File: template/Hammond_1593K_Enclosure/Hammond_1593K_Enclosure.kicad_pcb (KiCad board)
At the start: 2 copper layers, 56.6 x 57.7 mm, 4 parts

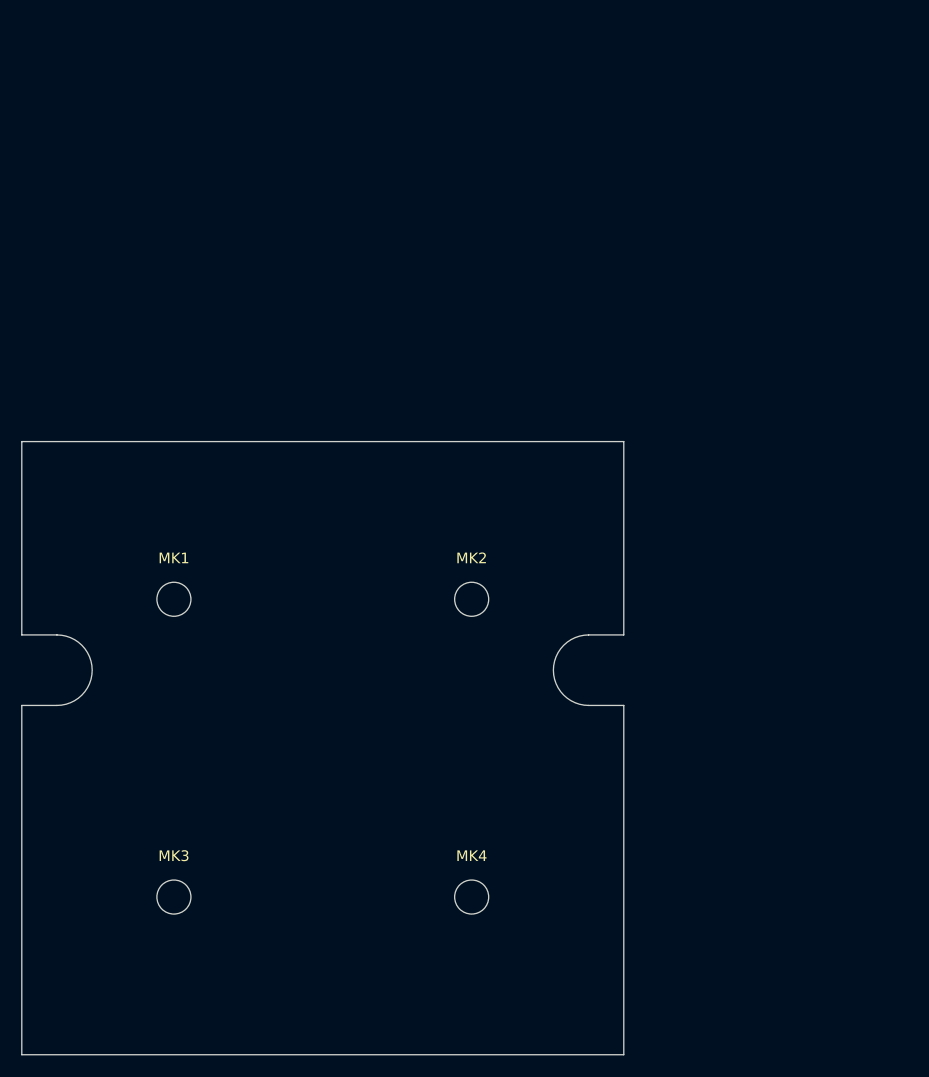
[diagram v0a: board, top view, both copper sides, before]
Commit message: fix: change original libs; add: new components
- Fix LIS3DH pins positions;
- Add ATmega164P symbol;
- Add 3D model to the L_Wuerth_HCM-7050;
- Add parameters for R_RES (Assembly...).
- Add parameters for R_RES and C_CAP;
- Fix SOIC-8 package 3D model;
- Add new parameters for many symbols;
- Change text height from 70 mil to 50 mil;
- Add solder mask expansion for 2-contact jumpers;
- Change thermopad vias of QFN-20-1EP_3x3mm_P0.45mm_EP1.6x1.6mm_ThermalVias;
- Add D_SMAF footprint;
- Fillet silk for C_1206;
-Rectangle silk for R_1206;
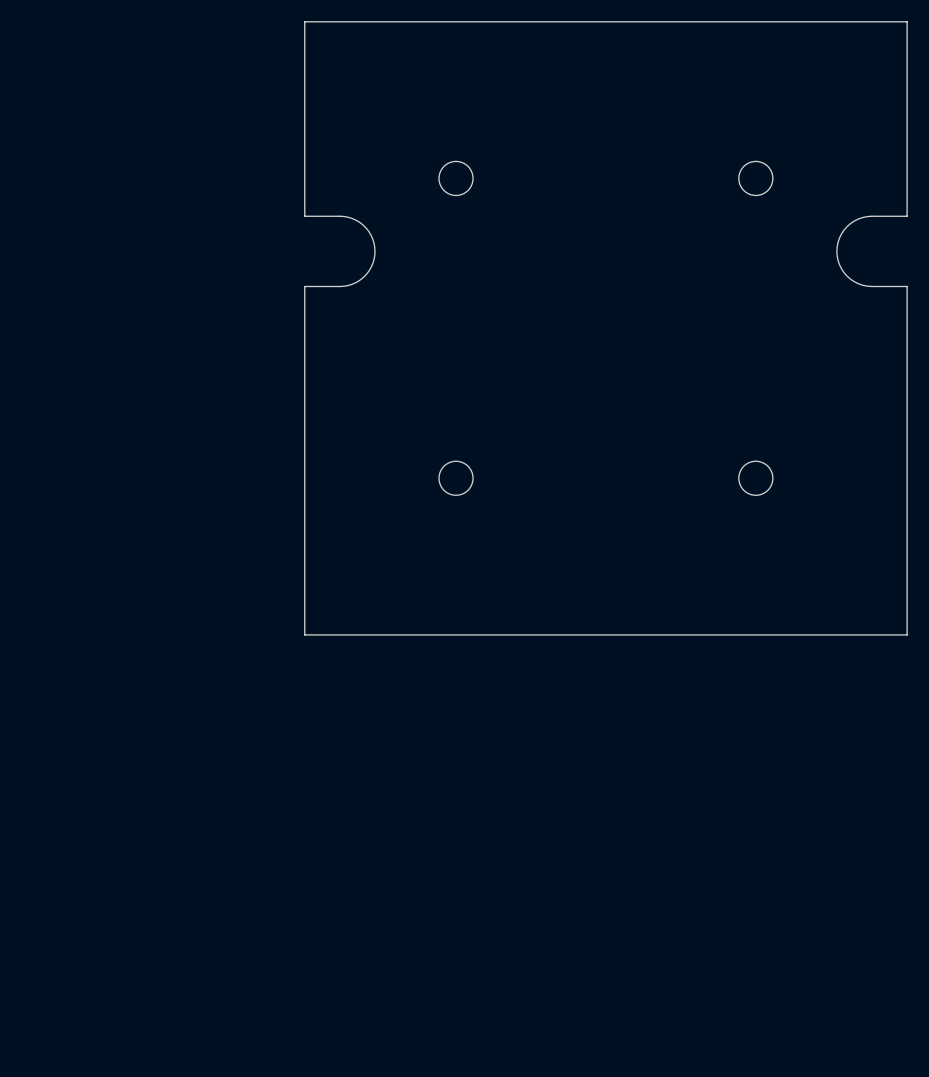
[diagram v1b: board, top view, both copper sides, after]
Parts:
- removed MK1, MK2, MK3, MK4: Mounting_Hole, Mounting_Holes:MountingHole_3.2mm_M3_ISO7380
- added MH1: MountingHole_3.2mm_M3_ISO7380, MountingHole:MountingHole_3.2mm_M3_ISO7380, F.Cu at (114.2, 57.1)
- added MH2: MountingHole_3.2mm_M3_ISO7380, MountingHole:MountingHole_3.2mm_M3_ISO7380, F.Cu at (114.2, 85.3)
- added MH3: MountingHole_3.2mm_M3_ISO7380, MountingHole:MountingHole_3.2mm_M3_ISO7380, F.Cu at (142.4, 57.1)
- added MH4: MountingHole_3.2mm_M3_ISO7380, MountingHole:MountingHole_3.2mm_M3_ISO7380, F.Cu at (142.4, 85.3)
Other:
- outline, holes or cut-outs redrawn
- board text removed: "NO CONNECTORS"
- board text removed: "RIGHT ANGLE CONNECTORS ON FRONT AND BACK ONLY"
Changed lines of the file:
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@@
-(kicad_pcb (version 20210126) (generator pcbnew)
+(kicad_pcb (version 20211014) (generator pcbnew)
   (general
     (thickness 1.6)
@@
     (33 "F.Adhes" user "F.Adhesive")
     (35 "F.Paste" user)
+    (36 "B.SilkS" user "B.Silkscreen")
     (37 "F.SilkS" user "F.Silkscreen")
+    (38 "B.Mask" user)
     (39 "F.Mask" user)
     (40 "Dwgs.User" user "User.Drawings")
@@
     (44 "Edge.Cuts" user)
     (45 "Margin" user)
+    (46 "B.CrtYd" user "B.Courtyard")
     (47 "F.CrtYd" user "F.Courtyard")
+    (48 "B.Fab" user)
     (49 "F.Fab" user)
   )
   (setup
-    (aux_axis_origin 130 100)
-    (grid_origin 130 100)
+    (stackup
+      (layer "F.SilkS" (type "Top Silk Screen"))
+      (layer "F.Paste" (type "Top Solder Paste"))
+      (layer "F.Mask" (type "Top Solder Mask") (color "Green") (thickness 0.01))
+      (layer "F.Cu" (type "copper") (thickness 0.035))
+      (layer "dielectric 1" (type "core") (thickness 1.51) (material "FR4") (epsilon_r 4.5) (loss_tangent 0.02))
+      (layer "B.Cu" (type "copper") (thickness 0.035))
+      (layer "B.Mask" (type "Bottom Solder Mask") (color "Green") (thickness 0.01))
+      (layer "B.SilkS" (type "Bottom Silk Screen"))
+      (copper_finish "None")
+      (dielectric_constraints no)
+    )
+    (pad_to_mask_clearance 0)
+    (aux_axis_origin 100 100)
+    (grid_origin 100 100)
     (pcbplotparams
       (layerselection 0x00010a8_80000001)
@@
   )
   (net 0 "")
-  (net 1 "Net-(MK1-Pad1)")
-  (net 2 "Net-(MK2-Pad1)")
-  (net 3 "Net-(MK3-Pad1)")
-  (net 4 "Net-(MK4-Pad1)")
-  (footprint "Mounting_Holes:MountingHole_3.2mm_M3_ISO7380" locked (layer "F.Cu")
-    (at 87.695 96.647)
+  (footprint "MountingHole:MountingHole_3.2mm_M3_ISO7380" locked (layer "F.Cu")
+    (at 142.418 85.268)
     (descr "Mounting Hole 3.2mm, no annular, M3, ISO7380")
     (tags "mounting hole 3.2mm no annular m3 iso7380")
-    (attr exclude_from_pos_files exclude_from_bom)
-    (fp_text reference "MK1" (at 0 -3.85) (layer "F.SilkS")
+    (attr board_only exclude_from_pos_files exclude_from_bom)
+    (fp_text reference "MH4" (at 0 -3.85) (layer "F.Fab") hide
       (effects (font (size 1 1) (thickness 0.15)))
     )
-    (fp_text value "Mounting_Hole" (at 0 3.85) (layer "F.Fab")
+    (fp_text value "MountingHole_3.2mm_M3_ISO7380" (at 0 3.85) (layer "F.Fab") hide
       (effects (font (size 1 1) (thickness 0.15)))
     )
-    (fp_text user "${REFERENCE}" (at 0.3 0) (layer "F.Fab")
+    (fp_text user "${REFERENCE}" (at 0.3 0) (layer "F.Fab") hide
       (effects (font (size 1 1) (thickness 0.15)))
     )
     (fp_circle (center 0 0) (end 2.85 0) (layer "Cmts.User") (width 0.15) (fill none))
     (fp_circle (center 0 0) (end 3.1 0) (layer "F.CrtYd") (width 0.05) (fill none))
-    (pad "1" np_thru_hole circle (at 0 0) (locked) (size 3.2 3.2) (drill 3.2) (layers *.Cu *.Mask)
-      (net 1 "Net-(MK1-Pad1)"))
+    (pad "" np_thru_hole circle locked (at 0 0) (size 3.2 3.2) (drill 3.2) (layers *.Cu *.Mask))
   )
-  (footprint "Mounting_Holes:MountingHole_3.2mm_M3_ISO7380" locked (layer "F.Cu")
-    (at 115.695 96.647)
+  (footprint "MountingHole:MountingHole_3.2mm_M3_ISO7380" locked (layer "F.Cu")
+    (at 114.224 85.268)
     (descr "Mounting Hole 3.2mm, no annular, M3, ISO7380")
     (tags "mounting hole 3.2mm no annular m3 iso7380")
-    (attr exclude_from_pos_files exclude_from_bom)
-    (fp_text reference "MK2" (at 0 -3.85) (layer "F.SilkS")
+    (attr board_only exclude_from_pos_files exclude_from_bom)
+    (fp_text reference "MH2" (at 0 -3.85) (layer "F.Fab") hide
       (effects (font (size 1 1) (thickness 0.15)))
     )
-    (fp_text value "Mounting_Hole" (at 0 3.85) (layer "F.Fab")
+    (fp_text value "MountingHole_3.2mm_M3_ISO7380" (at 0 3.85) (layer "F.Fab") hide
       (effects (font (size 1 1) (thickness 0.15)))
     )
-    (fp_text user "${REFERENCE}" (at 0.3 0) (layer "F.Fab")
+    (fp_text user "${REFERENCE}" (at 0.3 0) (layer "F.Fab") hide
       (effects (font (size 1 1) (thickness 0.15)))
     )
     (fp_circle (center 0 0) (end 2.85 0) (layer "Cmts.User") (width 0.15) (fill none))
     (fp_circle (center 0 0) (end 3.1 0) (layer "F.CrtYd") (width 0.05) (fill none))
-    (pad "1" np_thru_hole circle (at 0 0) (locked) (size 3.2 3.2) (drill 3.2) (layers *.Cu *.Mask)
-      (net 2 "Net-(MK2-Pad1)"))
+    (pad "" np_thru_hole circle locked (at 0 0) (size 3.2 3.2) (drill 3.2) (layers *.Cu *.Mask))
   )
-  (footprint "Mounting_Holes:MountingHole_3.2mm_M3_ISO7380" locked (layer "F.Cu")
-    (at 87.695 124.647)
+  (footprint "MountingHole:MountingHole_3.2mm_M3_ISO7380" locked (layer "F.Cu")
+    (at 142.418 57.074)
     (descr "Mounting Hole 3.2mm, no annular, M3, ISO7380")
     (tags "mounting hole 3.2mm no annular m3 iso7380")
-    (attr exclude_from_pos_files exclude_from_bom)
-    (fp_text reference "MK3" (at 0 -3.85) (layer "F.SilkS")
+    (attr board_only exclude_from_pos_files exclude_from_bom)
+    (fp_text reference "MH3" (at 0 -3.85) (layer "F.Fab") hide
       (effects (font (size 1 1) (thickness 0.15)))
     )
-    (fp_text value "Mounting_Hole" (at 0 3.85) (layer "F.Fab")
+    (fp_text value "MountingHole_3.2mm_M3_ISO7380" (at 0 3.85) (layer "F.Fab") hide
       (effects (font (size 1 1) (thickness 0.15)))
     )
-    (fp_text user "${REFERENCE}" (at 0.3 0) (layer "F.Fab")
+    (fp_text user "${REFERENCE}" (at 0.3 0) (layer "F.Fab") hide
       (effects (font (size 1 1) (thickness 0.15)))
     )
     (fp_circle (center 0 0) (end 2.85 0) (layer "Cmts.User") (width 0.15) (fill none))
     (fp_circle (center 0 0) (end 3.1 0) (layer "F.CrtYd") (width 0.05) (fill none))
-    (pad "1" np_thru_hole circle (at 0 0) (locked) (size 3.2 3.2) (drill 3.2) (layers *.Cu *.Mask)
-      (net 3 "Net-(MK3-Pad1)"))
+    (pad "" np_thru_hole circle locked (at 0 0) (size 3.2 3.2) (drill 3.2) (layers *.Cu *.Mask))
   )
-  (footprint "Mounting_Holes:MountingHole_3.2mm_M3_ISO7380" locked (layer "F.Cu")
-    (at 115.695 124.647)
+  (footprint "MountingHole:MountingHole_3.2mm_M3_ISO7380" locked (layer "F.Cu")
+    (at 114.224 57.074)
     (descr "Mounting Hole 3.2mm, no annular, M3, ISO7380")
     (tags "mounting hole 3.2mm no annular m3 iso7380")
-    (attr exclude_from_pos_files exclude_from_bom)
-    (fp_text reference "MK4" (at 0 -3.85) (layer "F.SilkS")
+    (attr board_only exclude_from_pos_files exclude_from_bom)
+    (fp_text reference "MH1" (at 0 -3.85) (layer "F.Fab") hide
       (effects (font (size 1 1) (thickness 0.15)))
     )
-    (fp_text value "Mounting_Hole" (at 0 3.85) (layer "F.Fab")
+    (fp_text value "MountingHole_3.2mm_M3_ISO7380" (at 0 3.85) (layer "F.Fab") hide
       (effects (font (size 1 1) (thickness 0.15)))
     )
-    (fp_text user "${REFERENCE}" (at 0.3 0) (layer "F.Fab")
+    (fp_text user "${REFERENCE}" (at 0.3 0) (layer "F.Fab") hide
       (effects (font (size 1 1) (thickness 0.15)))
     )
     (fp_circle (center 0 0) (end 2.85 0) (layer "Cmts.User") (width 0.15) (fill none))
     (fp_circle (center 0 0) (end 3.1 0) (layer "F.CrtYd") (width 0.05) (fill none))
-    (pad "1" np_thru_hole circle (at 0 0) (locked) (size 3.2 3.2) (drill 3.2) (layers *.Cu *.Mask)
-      (net 4 "Net-(MK4-Pad1)"))
+    (pad "" np_thru_hole circle locked (at 0 0) (size 3.2 3.2) (drill 3.2) (layers *.Cu *.Mask))
   )
-  (gr_arc (start 126.695 103.315) (end 126.695 106.63) (angle 180) (layer "Edge.Cuts") (width 0.1))
-  (gr_line (start 73.39 81.817) (end 73.39 100) (layer "Edge.Cuts") (width 0.1))
-  (gr_line (start 76.695 106.63) (end 73.39 106.63) (layer "Edge.Cuts") (width 0.1))
-  (gr_line (start 126.695 100) (end 130 100) (layer "Edge.Cuts") (width 0.1))
-  (gr_line (start 73.39 106.63) (end 73.39 139.477) (layer "Edge.Cuts") (width 0.1))
-  (gr_arc (start 76.695 103.315) (end 76.695 100) (angle 180) (layer "Edge.Cuts") (width 0.1))
-  (gr_line (start 130 81.817) (end 73.39 81.817) (layer "Edge.Cuts") (width 0.1))
-  (gr_line (start 130 100) (end 130 81.817) (layer "Edge.Cuts") (width 0.1))
-  (gr_line (start 130 139.477) (end 130 106.63) (layer "Edge.Cuts") (width 0.1))
-  (gr_line (start 130 106.63) (end 126.695 106.63) (layer "Edge.Cuts") (width 0.1))
-  (gr_line (start 73.39 100) (end 76.695 100) (layer "Edge.Cuts") (width 0.1))
-  (gr_line (start 73.39 139.477) (end 130 139.477) (layer "Edge.Cuts") (width 0.1))
-  (gr_text "NO CONNECTORS " (at 71 108 90) (layer "Dwgs.User")
-    (effects (font (size 1.5 1.5) (thickness 0.3)))
-  )
-  (gr_text "NO CONNECTORS " (at 133 108 90) (layer "Dwgs.User")
-    (effects (font (size 1.5 1.5) (thickness 0.3)))
-  )
-  (gr_text "RIGHT ANGLE CONNECTORS ON \nFRONT AND BACK ONLY" (at 102 143) (layer "Dwgs.User")
-    (effects (font (size 1.5 1.5) (thickness 0.3)))
-  )
+  (gr_line locked (start 100 60.63) (end 100 42.342) (layer "Edge.Cuts") (width 0.1))
+  (gr_arc locked (start 153.34 67.234) (mid 150.038 63.932) (end 153.34 60.63) (layer "Edge.Cuts") (width 0.1))
+  (gr_line locked (start 156.642 60.63) (end 156.642 42.342) (layer "Edge.Cuts") (width 0.1))
+  (gr_line locked (start 100 100) (end 156.642 100) (layer "Edge.Cuts") (width 0.1))
+  (gr_line locked (start 103.302 67.234) (end 100 67.234) (layer "Edge.Cuts") (width 0.1))
+  (gr_arc locked (start 103.302 60.63) (mid 106.604 63.932) (end 103.302 67.234) (layer "Edge.Cuts") (width 0.1))
+  (gr_line locked (start 153.34 67.234) (end 156.642 67.234) (layer "Edge.Cuts") (width 0.1))
+  (gr_line locked (start 103.302 60.63) (end 100 60.63) (layer "Edge.Cuts") (width 0.1))
+  (gr_line locked (start 100 67.234) (end 100 100) (layer "Edge.Cuts") (width 0.1))
+  (gr_line locked (start 156.642 42.342) (end 100 42.342) (layer "Edge.Cuts") (width 0.1))
+  (gr_line locked (start 153.34 60.63) (end 156.642 60.63) (layer "Edge.Cuts") (width 0.1))
+  (gr_line locked (start 156.642 100) (end 156.642 67.234) (layer "Edge.Cuts") (width 0.1))
 )
